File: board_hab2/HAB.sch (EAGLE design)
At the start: 31 parts

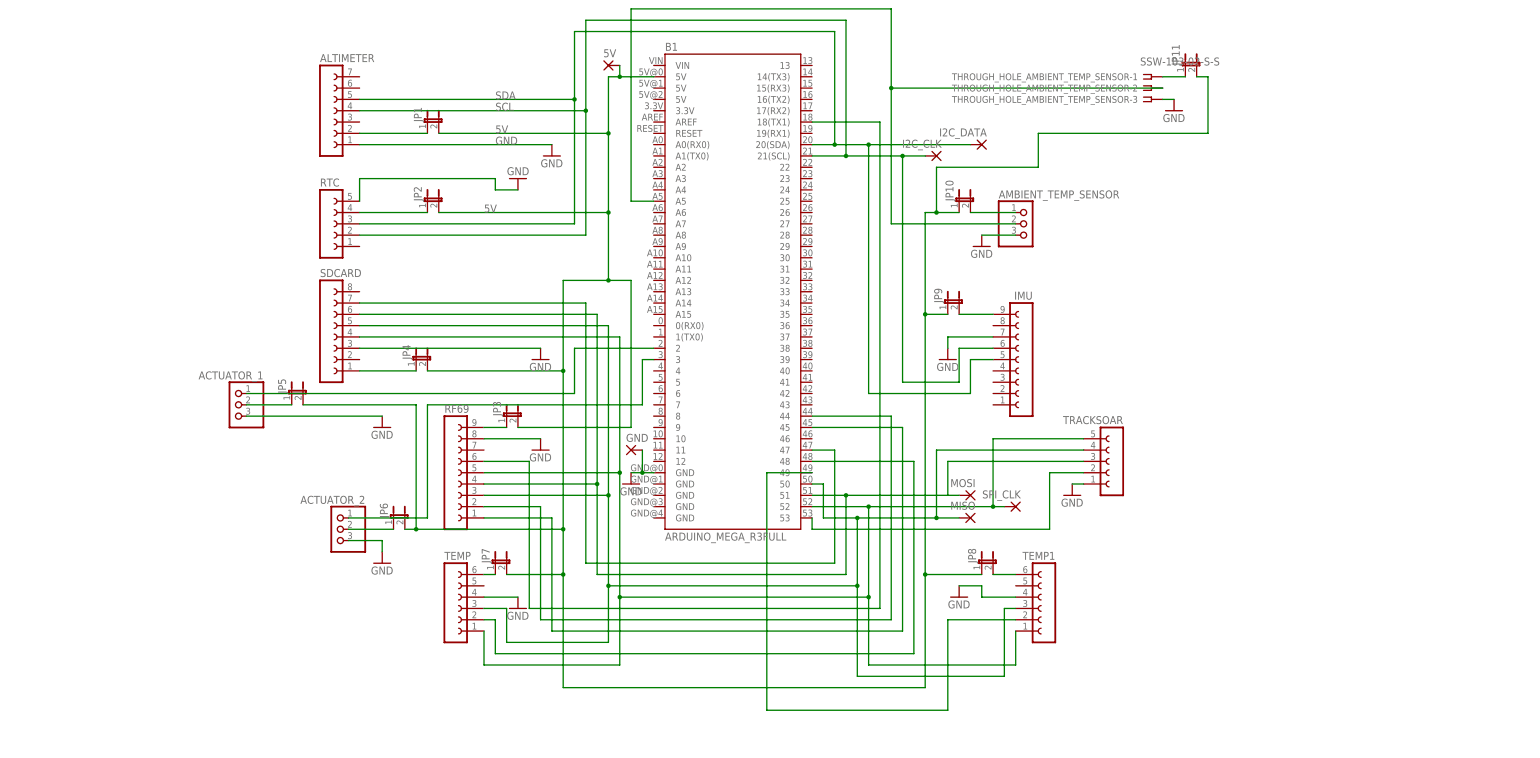
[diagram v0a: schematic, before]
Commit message: updated gitignore and added comments to HAB board
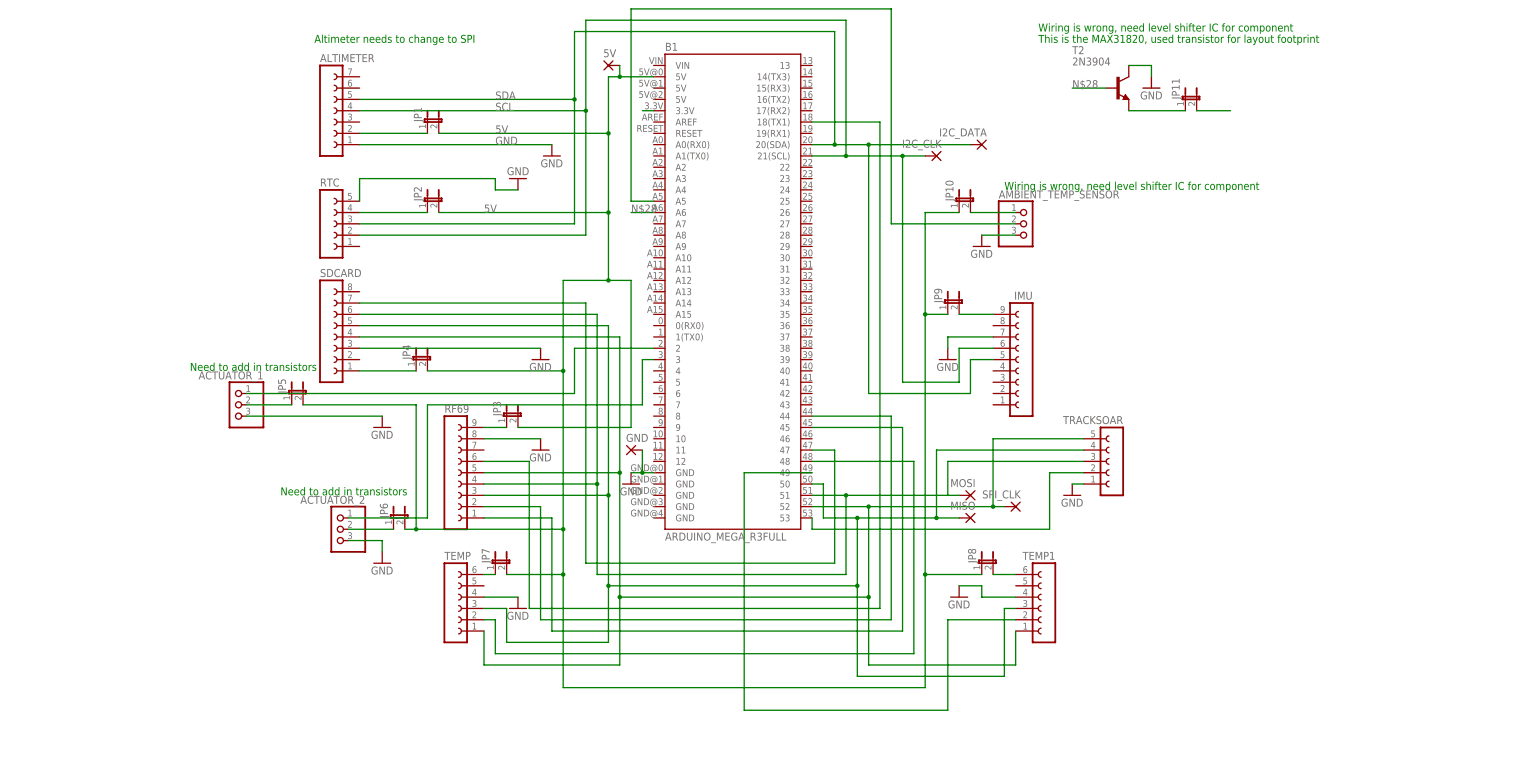
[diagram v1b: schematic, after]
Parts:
- removed THROUGH_HOLE_AMBIENT_TEMP_SENSOR: SSW-103-02-S-S, con-samtec:SSW-103-02-S-S
- added T2: 2N3904, transistor:2N3904
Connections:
- new net N$27: JP11.2
- new net N$28: B1.A6, T2.B
- new net N$29: B1.3.3V
- net 5V: no longer JP11.2
- net GND: now also T2.C; no longer THROUGH_HOLE_AMBIENT_TEMP_SENSOR-3.1
- net N$24: no longer THROUGH_HOLE_AMBIENT_TEMP_SENSOR-2.1
- net N$25: now also T2.E; no longer THROUGH_HOLE_AMBIENT_TEMP_SENSOR-1.1
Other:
- note added: "Altimeter needs to change to SPI"
- note added: "Need to add in transistors"
- note added: "This is the MAX31820, used transistor for layout footprint"
- note added: "Wiring is wrong, need level shifter IC for component"
- moved on the sheet: JP11
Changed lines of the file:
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@@
 <?xml version="1.0" encoding="utf-8"?>
 <!DOCTYPE eagle SYSTEM "eagle.dtd">
-<eagle version="8.3.2">
+<eagle version="8.7.1">
 <drawing>
 <settings>
@@
 <layers>
 <layer number="1" name="Top" color="4" fill="1" visible="no" active="no"/>
+<layer number="2" name="Route2" color="1" fill="3" visible="no" active="no"/>
+<layer number="3" name="Route3" color="4" fill="3" visible="no" active="no"/>
+<layer number="4" name="Route4" color="1" fill="4" visible="no" active="no"/>
+<layer number="5" name="Route5" color="4" fill="4" visible="no" active="no"/>
+<layer number="6" name="Route6" color="1" fill="8" visible="no" active="no"/>
+<layer number="7" name="Route7" color="4" fill="8" visible="no" active="no"/>
+<layer number="8" name="Route8" color="1" fill="2" visible="no" active="no"/>
+<layer number="9" name="Route9" color="4" fill="2" visible="no" active="no"/>
+<layer number="10" name="Route10" color="1" fill="7" visible="no" active="no"/>
+<layer number="11" name="Route11" color="4" fill="7" visible="no" active="no"/>
+<layer number="12" name="Route12" color="1" fill="5" visible="no" active="no"/>
+<layer number="13" name="Route13" color="4" fill="5" visible="no" active="no"/>
+<layer number="14" name="Route14" color="1" fill="6" visible="no" active="no"/>
+<layer number="15" name="Route15" color="4" fill="6" visible="no" active="no"/>
 <layer number="16" name="Bottom" color="1" fill="1" visible="no" active="no"/>
 <layer number="17" name="Pads" color="2" fill="1" visible="no" active="no"/>
@@
 <part name="TRACKSOAR" library="con-lsta" library_urn="urn:adsk.eagle:library:161" deviceset="FE05-1" device="" package3d_urn="urn:adsk.eagle:package:8190/1"/>
 <part name="GND12" library="supply1" library_urn="urn:adsk.eagle:library:371" deviceset="GND" device=""/>
-<part name="THROUGH_HOLE_AMBIENT_TEMP_SENSOR" library="con-samtec" library_urn="urn:adsk.eagle:library:184" deviceset="SSW-103-02-S-S" device=""/>
 <part name="JP11" library="jumper" library_urn="urn:adsk.eagle:library:252" deviceset="JP1E" device="" package3d_urn="urn:adsk.eagle:package:15455/1"/>
 <part name="GND13" library="supply1" library_urn="urn:adsk.eagle:library:371" deviceset="GND" device=""/>
+<part name="T2" library="transistor" library_urn="urn:adsk.eagle:library:402" deviceset="2N3904" device="" package3d_urn="urn:adsk.eagle:package:29893/2"/>
 </parts>
 <sheets>
 <sheet>
 <plain>
+<text x="119.38" y="99.06" size="1.778" layer="91">This is the MAX31820, used transistor for layout footprint</text>
+<text x="111.76" y="66.04" size="1.778" layer="91">Wiring is wrong, need level shifter IC for component</text>
+<text x="119.38" y="101.6" size="1.778" layer="91">Wiring is wrong, need level shifter IC for component</text>
+<text x="-71.12" y="25.4" size="1.778" layer="91">Need to add in transistors</text>
+<text x="-50.8" y="-2.54" size="1.778" layer="91">Need to add in transistors</text>
+<text x="-43.18" y="99.06" size="1.778" layer="91">Altimeter needs to change to SPI</text>
 </plain>
 <instances>
@@
 <instance part="TRACKSOAR" gate="G$1" x="137.16" y="5.08" rot="MR0"/>
 <instance part="GND12" gate="1" x="127" y="-2.54"/>
-<instance part="THROUGH_HOLE_AMBIENT_TEMP_SENSOR" gate="-1" x="144.78" y="91.44"/>
-<instance part="THROUGH_HOLE_AMBIENT_TEMP_SENSOR" gate="-2" x="144.78" y="88.9"/>
-<instance part="THROUGH_HOLE_AMBIENT_TEMP_SENSOR" gate="-3" x="144.78" y="86.36"/>
-<instance part="JP11" gate="A" x="152.4" y="93.98"/>
-<instance part="GND13" gate="1" x="149.86" y="83.82"/>
+<instance part="JP11" gate="A" x="152.4" y="86.36"/>
+<instance part="GND13" gate="1" x="144.78" y="88.9"/>
+<instance part="T2" gate="G1" x="137.16" y="88.9"/>
 </instances>
 <busses>
@@
 </segment>
 <segment>
-<pinref part="THROUGH_HOLE_AMBIENT_TEMP_SENSOR" gate="-3" pin="1"/>
 <pinref part="GND13" gate="1" pin="GND"/>
-<wire x1="147.32" y1="86.36" x2="149.86" y2="86.36" width="0.1524" layer="91"/>
+<pinref part="T2" gate="G1" pin="C"/>
+<wire x1="144.78" y1="91.44" x2="144.78" y2="93.98" width="0.1524" layer="91"/>
+<wire x1="144.78" y1="93.98" x2="139.7" y2="93.98" width="0.1524" layer="91"/>
 </segment>
 </net>
@@
 <junction x="93.98" y="38.1"/>
 <pinref part="JP10" gate="A" pin="1"/>
-<wire x1="93.98" y1="60.96" x2="96.52" y2="60.96" width="0.1524" layer="91"/>
-<pinref part="JP11" gate="A" pin="2"/>
-<wire x1="96.52" y1="60.96" x2="101.6" y2="60.96" width="0.1524" layer="91"/>
-<wire x1="154.94" y1="91.44" x2="157.48" y2="91.44" width="0.1524" layer="91"/>
-<wire x1="157.48" y1="91.44" x2="157.48" y2="78.74" width="0.1524" layer="91"/>
-<wire x1="157.48" y1="78.74" x2="119.38" y2="78.74" width="0.1524" layer="91"/>
-<wire x1="119.38" y1="78.74" x2="119.38" y2="71.12" width="0.1524" layer="91"/>
-<wire x1="119.38" y1="71.12" x2="96.52" y2="71.12" width="0.1524" layer="91"/>
-<wire x1="96.52" y1="71.12" x2="96.52" y2="60.96" width="0.1524" layer="91"/>
-<junction x="96.52" y="60.96"/>
+<wire x1="93.98" y1="60.96" x2="101.6" y2="60.96" width="0.1524" layer="91"/>
 </segment>
 </net>
@@
 <wire x1="27.94" y1="63.5" x2="27.94" y2="106.68" width="0.1524" layer="91"/>
 <wire x1="27.94" y1="106.68" x2="86.36" y2="106.68" width="0.1524" layer="91"/>
-<wire x1="86.36" y1="106.68" x2="86.36" y2="88.9" width="0.1524" layer="91"/>
-<pinref part="THROUGH_HOLE_AMBIENT_TEMP_SENSOR" gate="-2" pin="1"/>
-<wire x1="86.36" y1="88.9" x2="86.36" y2="58.42" width="0.1524" layer="91"/>
-<wire x1="147.32" y1="88.9" x2="86.36" y2="88.9" width="0.1524" layer="91"/>
-<junction x="86.36" y="88.9"/>
+<wire x1="86.36" y1="106.68" x2="86.36" y2="58.42" width="0.1524" layer="91"/>
 </segment>
 </net>
@@
 <segment>
 <pinref part="B1" gate="G$1" pin="49"/>
-<wire x1="58.42" y1="2.54" x2="68.58" y2="2.54" width="0.1524" layer="91"/>
+<wire x1="53.34" y1="2.54" x2="68.58" y2="2.54" width="0.1524" layer="91"/>
 <pinref part="TEMP1" gate="G$1" pin="2"/>
 <wire x1="99.06" y1="-30.48" x2="114.3" y2="-30.48" width="0.1524" layer="91"/>
 <wire x1="99.06" y1="-30.48" x2="99.06" y2="-50.8" width="0.1524" layer="91"/>
-<wire x1="99.06" y1="-50.8" x2="58.42" y2="-50.8" width="0.1524" layer="91"/>
-<wire x1="58.42" y1="-50.8" x2="58.42" y2="2.54" width="0.1524" layer="91"/>
+<wire x1="99.06" y1="-50.8" x2="53.34" y2="-50.8" width="0.1524" layer="91"/>
+<wire x1="53.34" y1="-50.8" x2="53.34" y2="2.54" width="0.1524" layer="91"/>
+</segment>
+</net>
+<net name="N$28" class="0">
+<segment>
+<pinref part="B1" gate="G$1" pin="A6"/>
+<wire x1="33.02" y1="60.96" x2="27.94" y2="60.96" width="0.1524" layer="91"/>
+<label x="27.94" y="60.96" size="1.778" layer="95"/>
+</segment>
+<segment>
+<label x="127" y="88.9" size="1.778" layer="95"/>
+<pinref part="T2" gate="G1" pin="B"/>
+<wire x1="127" y1="88.9" x2="134.62" y2="88.9" width="0.1524" layer="91"/>
 </segment>
 </net>
 <net name="N$25" class="0">
 <segment>
-<pinref part="THROUGH_HOLE_AMBIENT_TEMP_SENSOR" gate="-1" pin="1"/>
 <pinref part="JP11" gate="A" pin="1"/>
-<wire x1="147.32" y1="91.44" x2="152.4" y2="91.44" width="0.1524" layer="91"/>
-</segment>
-</net>
+<pinref part="T2" gate="G1" pin="E"/>
+<wire x1="152.4" y1="83.82" x2="139.7" y2="83.82" width="0.1524" layer="91"/>
+</segment>
+</net>
+<net name="N$27" class="0">
+<segment>
+<pinref part="JP11" gate="A" pin="2"/>
+<wire x1="154.94" y1="83.82" x2="162.56" y2="83.82" width="0.1524" layer="91"/>
+</segment>
+</net>
+<net name="N$29" class="0">
+<segment>
+<pinref part="B1" gate="G$1" pin="3.3V"/>
+<wire x1="33.02" y1="83.82" x2="30.48" y2="83.82" width="0.1524" layer="91"/>
+</segment>
+</net>

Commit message: Removed .DS_Store file and changed board schematics
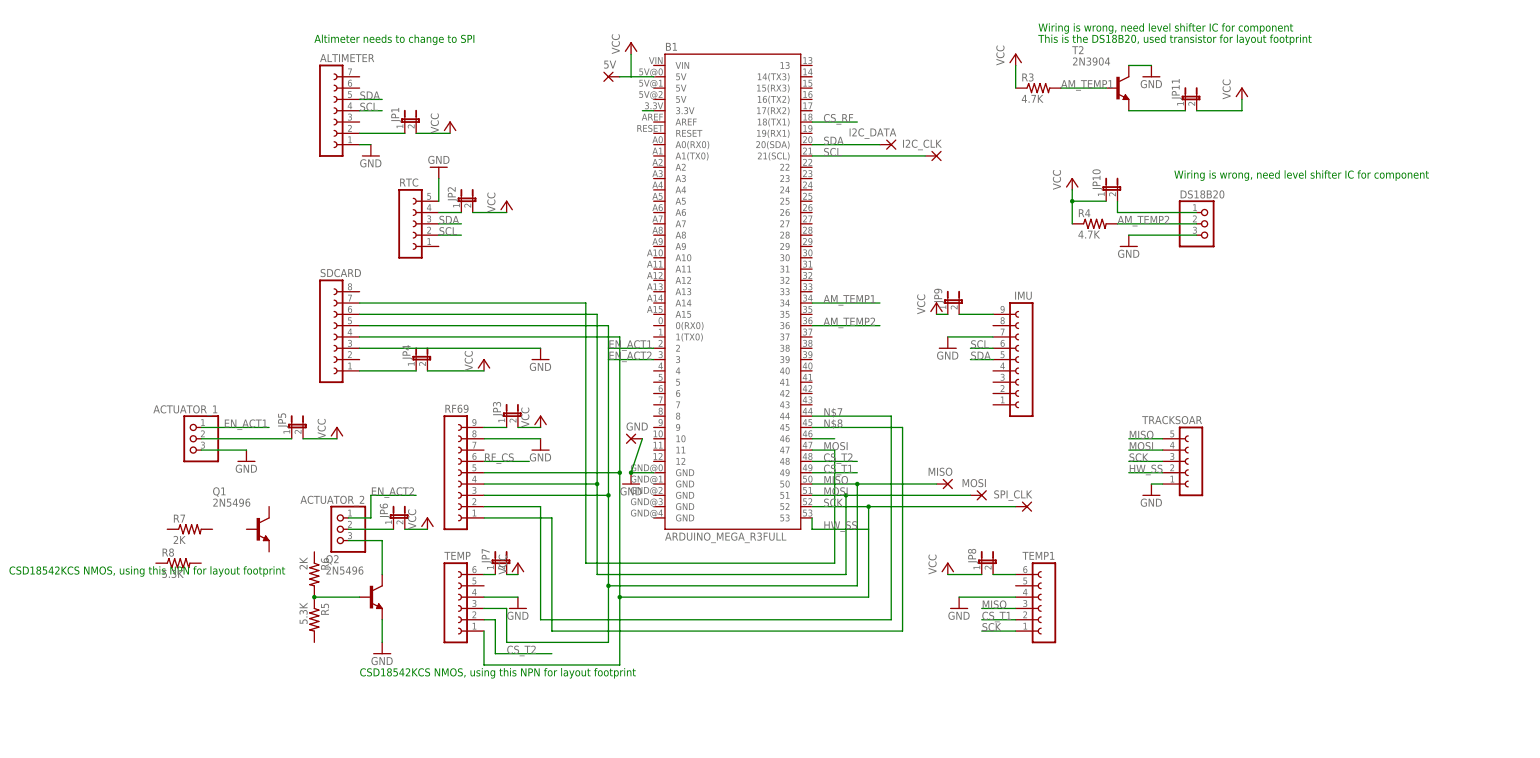
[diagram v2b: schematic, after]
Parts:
- removed AMBIENT_TEMP_SENSOR: (no value), adafruit:PINHD-1X3
- added DS18B20: (no value), adafruit:PINHD-1X3
- added Q1, Q2: 2N5496, transistor-npn:2N5496
- added R3, R4: 4.7K, rcl:R-US_0207/10
- added R5, R8: 5.3K, rcl:R-US_0207/10
- added R6, R7: 2K, rcl:R-US_0207/10
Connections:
- net N$10 renamed EN_ACT2
- net N$22 renamed HW_SS
- net N$23 renamed CS_T1
- net N$5 renamed CS_T2
- net N$9 renamed EN_ACT1
- removed net 5V: 5V.P, B1.5V@0, JP1.2, JP10.1, JP2.2, JP3.2, JP4.2, JP5.2, JP6.2, JP7.2, JP8.1, JP9.1
- removed net N$19: TEMP1.4
- removed net N$21: AMBIENT_TEMP_SENSOR.1, JP10.2
- removed net N$24: AMBIENT_TEMP_SENSOR.2, B1.A5
- removed net N$27: JP11.2
- removed net N$28: B1.A6, T2.B
- removed net N$4: B1.52, RF69.5, SDCARD.4, SPI_CLK.P, TEMP.1, TEMP1.1, TRACKSOAR.5
- removed net N$6: B1.18(TX1), RF69.6
- new net 1NAME: B1.46
- new net AM_TEMP1: B1.34, R3.2, T2.B
- new net AM_TEMP2: B1.36, DS18B20.2, R4.2
- new net CS_RF: B1.18(TX1)
- new net MISO: B1.50, MISO.P, RF69.3, SDCARD.5, TEMP.3, TEMP1.3, TRACKSOAR.5
- new net MOSI: B1.47, B1.51, MOSI.P, RF69.4, SDCARD.6, SDCARD.7, TRACKSOAR.4
- new net RF_CS: RF69.6
- new net SCK: B1.52, RF69.5, SDCARD.4, SPI_CLK.P, TEMP.1, TEMP1.1, TRACKSOAR.3
- new net VCC: 5V.P, B1.5V@0, JP1.2, JP10.1, JP11.2, JP2.2, JP3.2, JP4.2, JP5.2, JP6.2, JP7.2, JP8.1, JP9.1, R3.1, R4.1
- net GND: now also DS18B20.3, Q2.E, TEMP1.4; no longer ACTUATOR_2.3, AMBIENT_TEMP_SENSOR.3
- net N$1: now also Q2.B, R5.1, R6.2; no longer B1.47, SDCARD.7
- net N$2: now also DS18B20.1, JP10.2; no longer B1.51, MOSI.P, RF69.4, SDCARD.6, TRACKSOAR.3
- net N$3: now also ACTUATOR_2.3, Q2.C; no longer B1.50, MISO.P, RF69.3, SDCARD.5, TEMP.3, TEMP1.3, TRACKSOAR.4
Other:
- note added: "CSD18542KCS NMOS, using this NPN for layout footprint"
- note added: "This is the DS18B20, used transistor for layout footprint"
- note removed: "Need to add in transistors"
- note removed: "This is the MAX31820, used transistor for layout footprint"
- moved on the sheet: 5V, ACTUATOR_1, GND, I2C_DATA, JP1, JP10, JP2, JP5, MISO, MOSI, RTC, SPI_CLK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

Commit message: finished schematic
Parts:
- removed JP8: (no value), jumper:JP1E
- removed TEMP: (no value), con-lsta:FE06-1
- added JP12: (no value), jumper:JP1E
- added TEMP2: (no value), con-lsta:FE06-1
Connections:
- removed net 1NAME: B1.46
- removed net N$14: JP3.1, RF69.9
- removed net N$15: JP7.1, TEMP.6
- removed net N$18: JP8.2, TEMP1.6
- removed net RF_CS: RF69.6
- new net COM_ACT1: ACTUATOR_1.1, B1.2
- new net COM_ACT2: ACTUATOR_2.1, B1.3
- new net CS_SD: B1.47, SDCARD.7
- new net INT_RF: B1.18(TX1), RF69.4
- new net N$4: Q1.B, R7.1, R8.2
- new net N$5: ACTUATOR_1.3, Q1.C
- new net N$6: JP3.1, RF69.1
- new net RST_RF: B1.45, RF69.9
- net CS_RF: now also B1.44, RF69.8; no longer B1.18(TX1)
- net CS_T1: now also TEMP2.5; no longer TEMP1.2
- net CS_T2: now also TEMP1.5; no longer TEMP.2
- net EN_ACT1: now also R7.2; no longer ACTUATOR_1.1, B1.2
- net EN_ACT2: now also R6.1; no longer ACTUATOR_2.1, B1.3
- net GND: now also Q1.E, R5.2, R8.1, RF69.2, TEMP1.3, TEMP2.3; no longer ACTUATOR_1.3, RF69.8, TEMP.4, TEMP1.4
- net MISO: now also RF69.6, TEMP1.4, TEMP2.4; no longer RF69.3, TEMP.3, TEMP1.3
- net MOSI: now also RF69.7; no longer B1.47, RF69.4, SDCARD.7
- net N$7: now also JP7.1, TEMP1.1; no longer B1.44, RF69.2
- net N$8: now also JP12.1, TEMP2.1; no longer B1.45, RF69.1
- net SCK: now also TEMP1.6, TEMP2.6; no longer TEMP.1, TEMP1.1
- net VCC: now also JP12.2; no longer JP8.1
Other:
- note removed: "Altimeter needs to change to SPI"
- note removed: "Wiring is wrong, need level shifter IC for component"
- moved on the sheet: ACTUATOR_1, ACTUATOR_2, ALTIMETER, DS18B20, GND, IMU, JP1, JP10, JP11, JP2, JP3, JP4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
